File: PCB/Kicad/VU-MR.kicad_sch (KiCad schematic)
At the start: 32 parts, among them U10 SR2-MR, U9 SR1-MR

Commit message: PDF
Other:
- note added: "VU MASTER RIGHT"
- moved on the sheet: D76, D77, D78, D79, D80, D81, D82, D83, D84, D85, D86, D87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

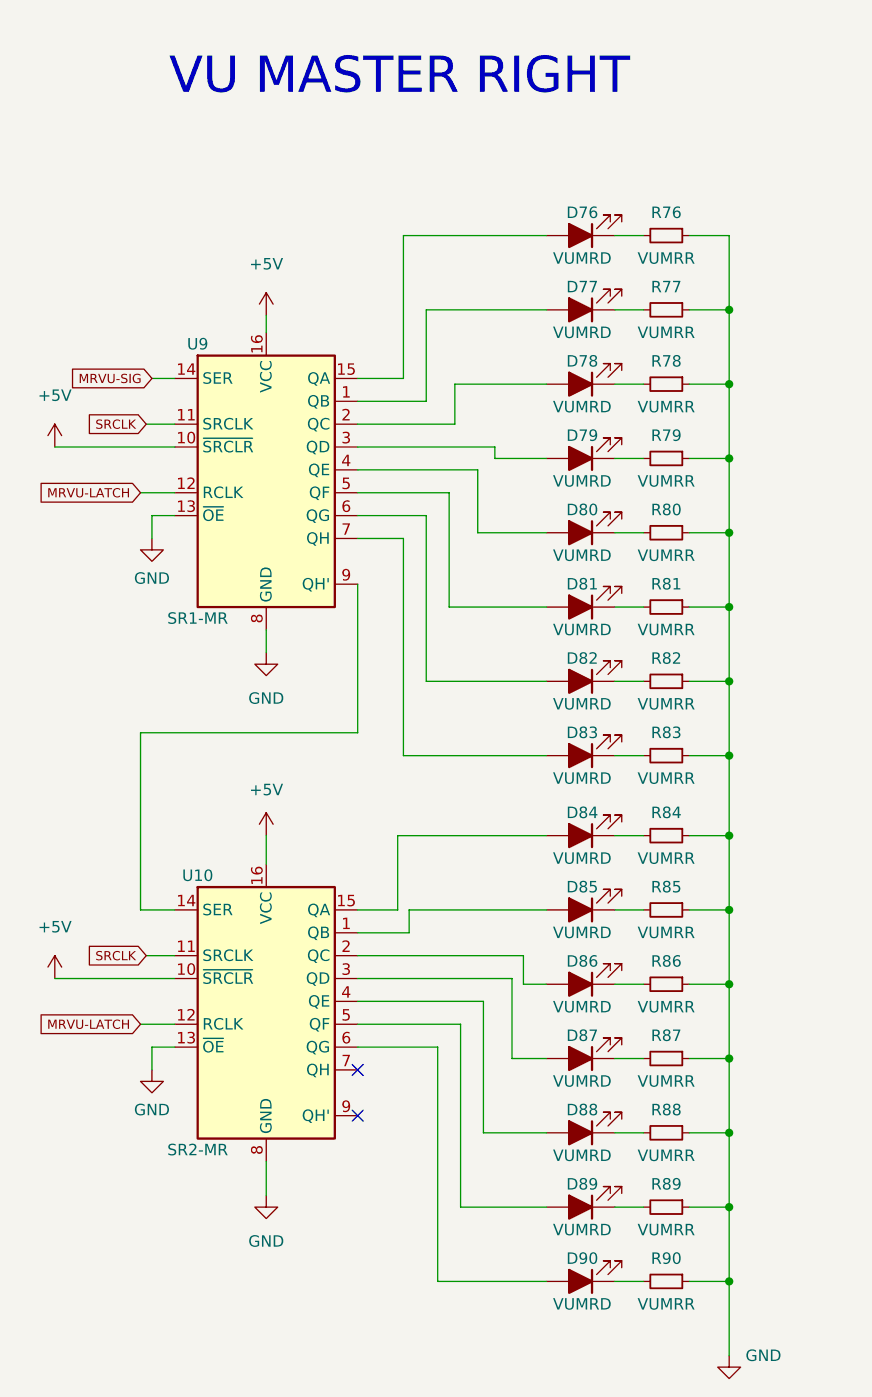
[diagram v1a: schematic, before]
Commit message: added transistor and 3x leds play- cue
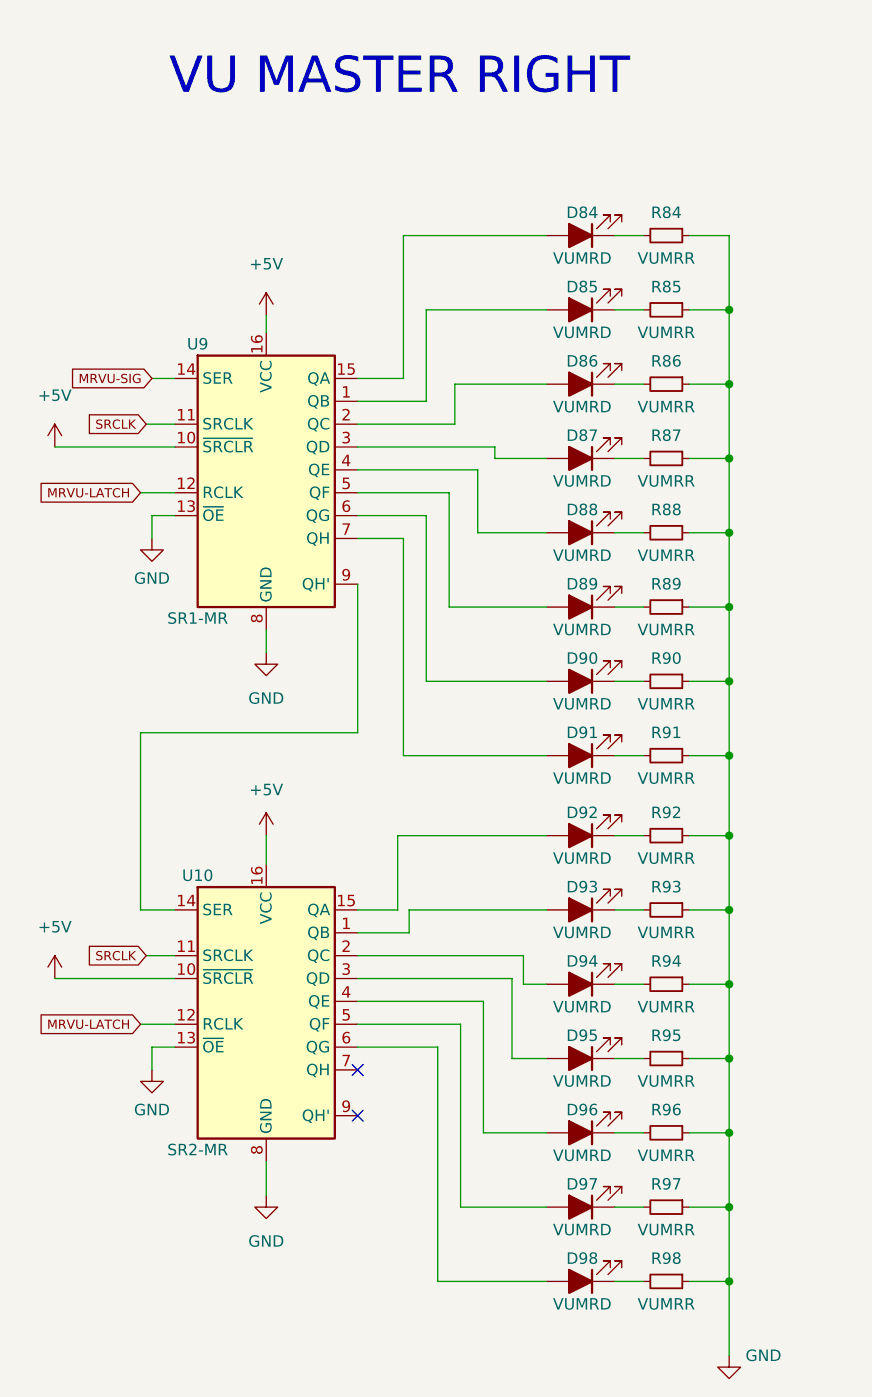
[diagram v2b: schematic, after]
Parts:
- U10, U9: footprint (none) -> Library:SO-16_3.9x9.9mm_P1.27mm
- renumbered D76 to D84, D77 to D85, D78 to D86, D79 to D87, D80 to D88, D81 to D89, D82 to D90, D83 to D91, D84 to D92, D85 to D93, D86 to D94, D87 to D95, D88 to D96, D89 to D97, D90 to D98, R76 to R84, R77 to R85, R78 to R86, R79 to R87, R80 to R88, R81 to R89, R82 to R90, R83 to R91, R84 to R92, R85 to R93, R86 to R94, R87 to R95, R88 to R96, R89 to R97, R90 to R98

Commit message: routing WIP
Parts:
- D93, D94, D95, D96: footprint Library:LED_GREEN -> Library:LED_YELLOW
- D97, D98: footprint Library:LED_GREEN -> Library:LED_RED
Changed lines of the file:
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@@
     (property "Reference" "D93" (id 0) (at 116.3955 121.285 0))
     (property "Value" "VUMRD" (id 1) (at 116.3955 126.365 0))
-    (property "Footprint" "Library:LED_GREEN" (id 2) (at 116.205 123.825 0)
+    (property "Footprint" "Library:LED_YELLOW" (id 2) (at 116.205 123.825 0)
       (effects (font (size 1.27 1.27)) hide)
     )
@@
     (property "Reference" "D94" (id 0) (at 116.3955 129.54 0))
     (property "Value" "VUMRD" (id 1) (at 116.3955 134.62 0))
-    (property "Footprint" "Library:LED_GREEN" (id 2) (at 116.205 132.08 0)
+    (property "Footprint" "Library:LED_YELLOW" (id 2) (at 116.205 132.08 0)
       (effects (font (size 1.27 1.27)) hide)
     )
@@
     (property "Reference" "D95" (id 0) (at 116.3955 137.795 0))
     (property "Value" "VUMRD" (id 1) (at 116.3955 142.875 0))
-    (property "Footprint" "Library:LED_GREEN" (id 2) (at 116.205 140.335 0)
+    (property "Footprint" "Library:LED_YELLOW" (id 2) (at 116.205 140.335 0)
       (effects (font (size 1.27 1.27)) hide)
     )
@@
     (property "Reference" "D96" (id 0) (at 116.3955 146.05 0))
     (property "Value" "VUMRD" (id 1) (at 116.3955 151.13 0))
-    (property "Footprint" "Library:LED_GREEN" (id 2) (at 116.205 148.59 0)
+    (property "Footprint" "Library:LED_YELLOW" (id 2) (at 116.205 148.59 0)
       (effects (font (size 1.27 1.27)) hide)
     )
@@
     (property "Reference" "D97" (id 0) (at 116.3955 154.305 0))
     (property "Value" "VUMRD" (id 1) (at 116.3955 159.385 0))
-    (property "Footprint" "Library:LED_GREEN" (id 2) (at 116.205 156.845 0)
+    (property "Footprint" "Library:LED_RED" (id 2) (at 116.205 156.845 0)
       (effects (font (size 1.27 1.27)) hide)
     )
@@
     (property "Reference" "D98" (id 0) (at 116.3955 162.56 0))
     (property "Value" "VUMRD" (id 1) (at 116.3955 167.64 0))
-    (property "Footprint" "Library:LED_GREEN" (id 2) (at 116.205 165.1 0)
+    (property "Footprint" "Library:LED_RED" (id 2) (at 116.205 165.1 0)
       (effects (font (size 1.27 1.27)) hide)
     )

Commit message: routes finished
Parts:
- D84, D85: footprint Library:LED_GREEN -> Library:LED_RED
- D86, D87, D88, D89: footprint Library:LED_GREEN -> Library:LED_YELLOW
- D93, D94, D95, D96: footprint Library:LED_YELLOW -> Library:LED_GREEN
- D97, D98: footprint Library:LED_RED -> Library:LED_GREEN
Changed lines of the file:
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@@
-(kicad_sch (version 20210615) (generator eeschema)
+(kicad_sch (version 20210621) (generator eeschema)
   (paper "A4")
   (junction (at 132.715 57.15) (diameter 0.9144) (color 0 0 0 0))
@@
     (property "Reference" "D84" (id 0) (at 116.3955 46.355 0))
     (property "Value" "VUMRD" (id 1) (at 116.3955 51.435 0))
-    (property "Footprint" "Library:LED_GREEN" (id 2) (at 116.205 48.895 0)
+    (property "Footprint" "Library:LED_RED" (id 2) (at 116.205 48.895 0)
       (effects (font (size 1.27 1.27)) hide)
     )
@@
     (property "Reference" "D85" (id 0) (at 116.3955 54.61 0))
     (property "Value" "VUMRD" (id 1) (at 116.3955 59.69 0))
-    (property "Footprint" "Library:LED_GREEN" (id 2) (at 116.205 57.15 0)
+    (property "Footprint" "Library:LED_RED" (id 2) (at 116.205 57.15 0)
       (effects (font (size 1.27 1.27)) hide)
     )
@@
     (property "Reference" "D86" (id 0) (at 116.3955 62.865 0))
     (property "Value" "VUMRD" (id 1) (at 116.3955 67.945 0))
-    (property "Footprint" "Library:LED_GREEN" (id 2) (at 116.205 65.405 0)
+    (property "Footprint" "Library:LED_YELLOW" (id 2) (at 116.205 65.405 0)
       (effects (font (size 1.27 1.27)) hide)
     )
@@
     (property "Reference" "D87" (id 0) (at 116.3955 71.12 0))
     (property "Value" "VUMRD" (id 1) (at 116.3955 76.2 0))
-    (property "Footprint" "Library:LED_GREEN" (id 2) (at 116.205 73.66 0)
+    (property "Footprint" "Library:LED_YELLOW" (id 2) (at 116.205 73.66 0)
       (effects (font (size 1.27 1.27)) hide)
     )
@@
     (property "Reference" "D88" (id 0) (at 116.3955 79.375 0))
     (property "Value" "VUMRD" (id 1) (at 116.3955 84.455 0))
-    (property "Footprint" "Library:LED_GREEN" (id 2) (at 116.205 81.915 0)
+    (property "Footprint" "Library:LED_YELLOW" (id 2) (at 116.205 81.915 0)
       (effects (font (size 1.27 1.27)) hide)
     )
@@
     (property "Reference" "D89" (id 0) (at 116.3955 87.63 0))
     (property "Value" "VUMRD" (id 1) (at 116.3955 92.71 0))
-    (property "Footprint" "Library:LED_GREEN" (id 2) (at 116.205 90.17 0)
+    (property "Footprint" "Library:LED_YELLOW" (id 2) (at 116.205 90.17 0)
       (effects (font (size 1.27 1.27)) hide)
     )
@@
     (property "Reference" "D93" (id 0) (at 116.3955 121.285 0))
     (property "Value" "VUMRD" (id 1) (at 116.3955 126.365 0))
-    (property "Footprint" "Library:LED_YELLOW" (id 2) (at 116.205 123.825 0)
+    (property "Footprint" "Library:LED_GREEN" (id 2) (at 116.205 123.825 0)
       (effects (font (size 1.27 1.27)) hide)
     )
@@
     (property "Reference" "D94" (id 0) (at 116.3955 129.54 0))
     (property "Value" "VUMRD" (id 1) (at 116.3955 134.62 0))
-    (property "Footprint" "Library:LED_YELLOW" (id 2) (at 116.205 132.08 0)
+    (property "Footprint" "Library:LED_GREEN" (id 2) (at 116.205 132.08 0)
       (effects (font (size 1.27 1.27)) hide)
     )
@@
     (property "Reference" "D95" (id 0) (at 116.3955 137.795 0))
     (property "Value" "VUMRD" (id 1) (at 116.3955 142.875 0))
-    (property "Footprint" "Library:LED_YELLOW" (id 2) (at 116.205 140.335 0)
+    (property "Footprint" "Library:LED_GREEN" (id 2) (at 116.205 140.335 0)
       (effects (font (size 1.27 1.27)) hide)
     )
@@
     (property "Reference" "D96" (id 0) (at 116.3955 146.05 0))
     (property "Value" "VUMRD" (id 1) (at 116.3955 151.13 0))
-    (property "Footprint" "Library:LED_YELLOW" (id 2) (at 116.205 148.59 0)
+    (property "Footprint" "Library:LED_GREEN" (id 2) (at 116.205 148.59 0)
       (effects (font (size 1.27 1.27)) hide)
     )
@@
     (property "Reference" "D97" (id 0) (at 116.3955 154.305 0))
     (property "Value" "VUMRD" (id 1) (at 116.3955 159.385 0))
-    (property "Footprint" "Library:LED_RED" (id 2) (at 116.205 156.845 0)
+    (property "Footprint" "Library:LED_GREEN" (id 2) (at 116.205 156.845 0)
       (effects (font (size 1.27 1.27)) hide)
     )
@@
     (property "Reference" "D98" (id 0) (at 116.3955 162.56 0))
     (property "Value" "VUMRD" (id 1) (at 116.3955 167.64 0))
-    (property "Footprint" "Library:LED_RED" (id 2) (at 116.205 165.1 0)
-      (effects (font (size 1.27 1.27)) hide)
-    )
+    (property "Footprint" "Library:LED_GREEN" (id 2) (at 116.205 165.1 0)
+      (effects (font (size 1.27 1.27)) hide)
+    )

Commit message: update schematic
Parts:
- R84, R85, R86, R87, R88, R89, R90, R91, R92, R93, R94, R95, R96, R97, R98: footprint Library:R_1206_3216Metric_Pad1.30x1.75mm_HandSolder -> Resistor_SMD:R_1206_3216Metric_Pad1.30x1.75mm_HandSolder
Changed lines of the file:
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@@
     (property "Reference" "R84" (id 0) (at 125.73 46.355 90))
     (property "Value" "VUMRR" (id 1) (at 125.73 51.435 90))
-    (property "Footprint" "Library:R_1206_3216Metric_Pad1.30x1.75mm_HandSolder" (id 2) (at 125.73 48.895 0)
+    (property "Footprint" "Resistor_SMD:R_1206_3216Metric_Pad1.30x1.75mm_HandSolder" (id 2) (at 125.73 48.895 0)
       (effects (font (size 1.27 1.27)) hide)
     )
@@
     (property "Reference" "R85" (id 0) (at 125.73 54.61 90))
     (property "Value" "VUMRR" (id 1) (at 125.73 59.69 90))
-    (property "Footprint" "Library:R_1206_3216Metric_Pad1.30x1.75mm_HandSolder" (id 2) (at 125.73 57.15 0)
+    (property "Footprint" "Resistor_SMD:R_1206_3216Metric_Pad1.30x1.75mm_HandSolder" (id 2) (at 125.73 57.15 0)
       (effects (font (size 1.27 1.27)) hide)
     )
@@
     (property "Reference" "R86" (id 0) (at 125.73 62.865 90))
     (property "Value" "VUMRR" (id 1) (at 125.73 67.945 90))
-    (property "Footprint" "Library:R_1206_3216Metric_Pad1.30x1.75mm_HandSolder" (id 2) (at 125.73 65.405 0)
+    (property "Footprint" "Resistor_SMD:R_1206_3216Metric_Pad1.30x1.75mm_HandSolder" (id 2) (at 125.73 65.405 0)
       (effects (font (size 1.27 1.27)) hide)
     )
@@
     (property "Reference" "R87" (id 0) (at 125.73 71.12 90))
     (property "Value" "VUMRR" (id 1) (at 125.73 76.2 90))
-    (property "Footprint" "Library:R_1206_3216Metric_Pad1.30x1.75mm_HandSolder" (id 2) (at 125.73 73.66 0)
+    (property "Footprint" "Resistor_SMD:R_1206_3216Metric_Pad1.30x1.75mm_HandSolder" (id 2) (at 125.73 73.66 0)
       (effects (font (size 1.27 1.27)) hide)
     )
@@
     (property "Reference" "R88" (id 0) (at 125.73 79.375 90))
     (property "Value" "VUMRR" (id 1) (at 125.73 84.455 90))
-    (property "Footprint" "Library:R_1206_3216Metric_Pad1.30x1.75mm_HandSolder" (id 2) (at 125.73 81.915 0)
+    (property "Footprint" "Resistor_SMD:R_1206_3216Metric_Pad1.30x1.75mm_HandSolder" (id 2) (at 125.73 81.915 0)
       (effects (font (size 1.27 1.27)) hide)
     )
@@
     (property "Reference" "R89" (id 0) (at 125.73 87.63 90))
     (property "Value" "VUMRR" (id 1) (at 125.73 92.71 90))
-    (property "Footprint" "Library:R_1206_3216Metric_Pad1.30x1.75mm_HandSolder" (id 2) (at 125.73 90.17 0)
+    (property "Footprint" "Resistor_SMD:R_1206_3216Metric_Pad1.30x1.75mm_HandSolder" (id 2) (at 125.73 90.17 0)
       (effects (font (size 1.27 1.27)) hide)
     )
@@
     (property "Reference" "R90" (id 0) (at 125.73 95.885 90))
     (property "Value" "VUMRR" (id 1) (at 125.73 100.965 90))
-    (property "Footprint" "Library:R_1206_3216Metric_Pad1.30x1.75mm_HandSolder" (id 2) (at 125.73 98.425 0)
+    (property "Footprint" "Resistor_SMD:R_1206_3216Metric_Pad1.30x1.75mm_HandSolder" (id 2) (at 125.73 98.425 0)
       (effects (font (size 1.27 1.27)) hide)
     )
@@
     (property "Reference" "R91" (id 0) (at 125.73 104.14 90))
     (property "Value" "VUMRR" (id 1) (at 125.73 109.22 90))
-    (property "Footprint" "Library:R_1206_3216Metric_Pad1.30x1.75mm_HandSolder" (id 2) (at 125.73 106.68 0)
+    (property "Footprint" "Resistor_SMD:R_1206_3216Metric_Pad1.30x1.75mm_HandSolder" (id 2) (at 125.73 106.68 0)
       (effects (font (size 1.27 1.27)) hide)
     )
@@
     (property "Reference" "R92" (id 0) (at 125.73 113.03 90))
     (property "Value" "VUMRR" (id 1) (at 125.73 118.11 90))
-    (property "Footprint" "Library:R_1206_3216Metric_Pad1.30x1.75mm_HandSolder" (id 2) (at 125.73 115.57 0)
+    (property "Footprint" "Resistor_SMD:R_1206_3216Metric_Pad1.30x1.75mm_HandSolder" (id 2) (at 125.73 115.57 0)
       (effects (font (size 1.27 1.27)) hide)
     )
@@
     (property "Reference" "R93" (id 0) (at 125.73 121.285 90))
     (property "Value" "VUMRR" (id 1) (at 125.73 126.365 90))
-    (property "Footprint" "Library:R_1206_3216Metric_Pad1.30x1.75mm_HandSolder" (id 2) (at 125.73 123.825 0)
+    (property "Footprint" "Resistor_SMD:R_1206_3216Metric_Pad1.30x1.75mm_HandSolder" (id 2) (at 125.73 123.825 0)
       (effects (font (size 1.27 1.27)) hide)
     )
@@
     (property "Reference" "R94" (id 0) (at 125.73 129.54 90))
     (property "Value" "VUMRR" (id 1) (at 125.73 134.62 90))
-    (property "Footprint" "Library:R_1206_3216Metric_Pad1.30x1.75mm_HandSolder" (id 2) (at 125.73 132.08 0)
+    (property "Footprint" "Resistor_SMD:R_1206_3216Metric_Pad1.30x1.75mm_HandSolder" (id 2) (at 125.73 132.08 0)
       (effects (font (size 1.27 1.27)) hide)
     )
@@
     (property "Reference" "R95" (id 0) (at 125.73 137.795 90))
     (property "Value" "VUMRR" (id 1) (at 125.73 142.875 90))
-    (property "Footprint" "Library:R_1206_3216Metric_Pad1.30x1.75mm_HandSolder" (id 2) (at 125.73 140.335 0)
+    (property "Footprint" "Resistor_SMD:R_1206_3216Metric_Pad1.30x1.75mm_HandSolder" (id 2) (at 125.73 140.335 0)
       (effects (font (size 1.27 1.27)) hide)
     )
@@
     (property "Reference" "R96" (id 0) (at 125.73 146.05 90))
     (property "Value" "VUMRR" (id 1) (at 125.73 151.13 90))
-    (property "Footprint" "Library:R_1206_3216Metric_Pad1.30x1.75mm_HandSolder" (id 2) (at 125.73 148.59 0)
+    (property "Footprint" "Resistor_SMD:R_1206_3216Metric_Pad1.30x1.75mm_HandSolder" (id 2) (at 125.73 148.59 0)
       (effects (font (size 1.27 1.27)) hide)
     )
@@
     (property "Reference" "R97" (id 0) (at 125.73 154.305 90))
     (property "Value" "VUMRR" (id 1) (at 125.73 159.385 90))
-    (property "Footprint" "Library:R_1206_3216Metric_Pad1.30x1.75mm_HandSolder" (id 2) (at 125.73 156.845 0)
+    (property "Footprint" "Resistor_SMD:R_1206_3216Metric_Pad1.30x1.75mm_HandSolder" (id 2) (at 125.73 156.845 0)
       (effects (font (size 1.27 1.27)) hide)
     )
@@
     (property "Reference" "R98" (id 0) (at 125.73 162.56 90))
     (property "Value" "VUMRR" (id 1) (at 125.73 167.64 90))
-    (property "Footprint" "Library:R_1206_3216Metric_Pad1.30x1.75mm_HandSolder" (id 2) (at 125.73 165.1 0)
+    (property "Footprint" "Resistor_SMD:R_1206_3216Metric_Pad1.30x1.75mm_HandSolder" (id 2) (at 125.73 165.1 0)
       (effects (font (size 1.27 1.27)) hide)
     )

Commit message: modified trillbar connectors
Signed-off-by: Jose Vega <josevega234@gmail.com>
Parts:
- U10, U9: footprint Library:SO-16_3.9x9.9mm_P1.27mm -> Package_SO:SOIC-16_3.9x9.9mm_P1.27mm
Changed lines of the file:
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@@
-(kicad_sch (version 20210621) (generator eeschema)
+(kicad_sch (version 20210615) (generator eeschema)
   (paper "A4")
   (junction (at 132.715 57.15) (diameter 0.9144) (color 0 0 0 0))
@@
     (property "Reference" "U9" (id 0) (at 73.66 60.96 0))
     (property "Value" "SR1-MR" (id 1) (at 73.66 91.44 0))
-    (property "Footprint" "Library:SO-16_3.9x9.9mm_P1.27mm" (id 2) (at 81.28 74.93 0)
+    (property "Footprint" "Package_SO:SOIC-16_3.9x9.9mm_P1.27mm" (id 2) (at 81.28 74.93 0)
       (effects (font (size 1.27 1.27)) hide)
     )
@@
     (property "Reference" "U10" (id 0) (at 73.66 120.015 0))
     (property "Value" "SR2-MR" (id 1) (at 73.66 150.495 0))
-    (property "Footprint" "Library:SO-16_3.9x9.9mm_P1.27mm" (id 2) (at 81.28 133.985 0)
-      (effects (font (size 1.27 1.27)) hide)
-    )
+    (property "Footprint" "Package_SO:SOIC-16_3.9x9.9mm_P1.27mm" (id 2) (at 81.28 133.985 0)
+      (effects (font (size 1.27 1.27)) hide)
+    )
